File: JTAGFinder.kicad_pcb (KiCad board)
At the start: 4 copper layers, 90 x 70 mm, 95 parts, among them J1 Conn_02x05_Odd_Even, J10 V_drive, J2 Conn_02x05_Odd_Even, J3 LCD_IIC, J4 USB_C_Receptacle_USB2.0, J5 BT_HC08_SERIAL_COM, J6 Bus_PCI_Express_x1_free_pins_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, J7 GND, J8 GPIO_19-23, J9 +3V3, Q1 2N3904, SW1 SW_Push, U11 SN74S1051, U12 SN74S1051, U13 P8X32A-Q44, U2 M24512E-FMN6TP, U3 MIC2025-2YM, U4 FT232RL, U5 TLV74033, U6 USBLC6-2SC6, U7 AD8655, U8 LFS0108, U9 LFS0108, Y1 5MHz

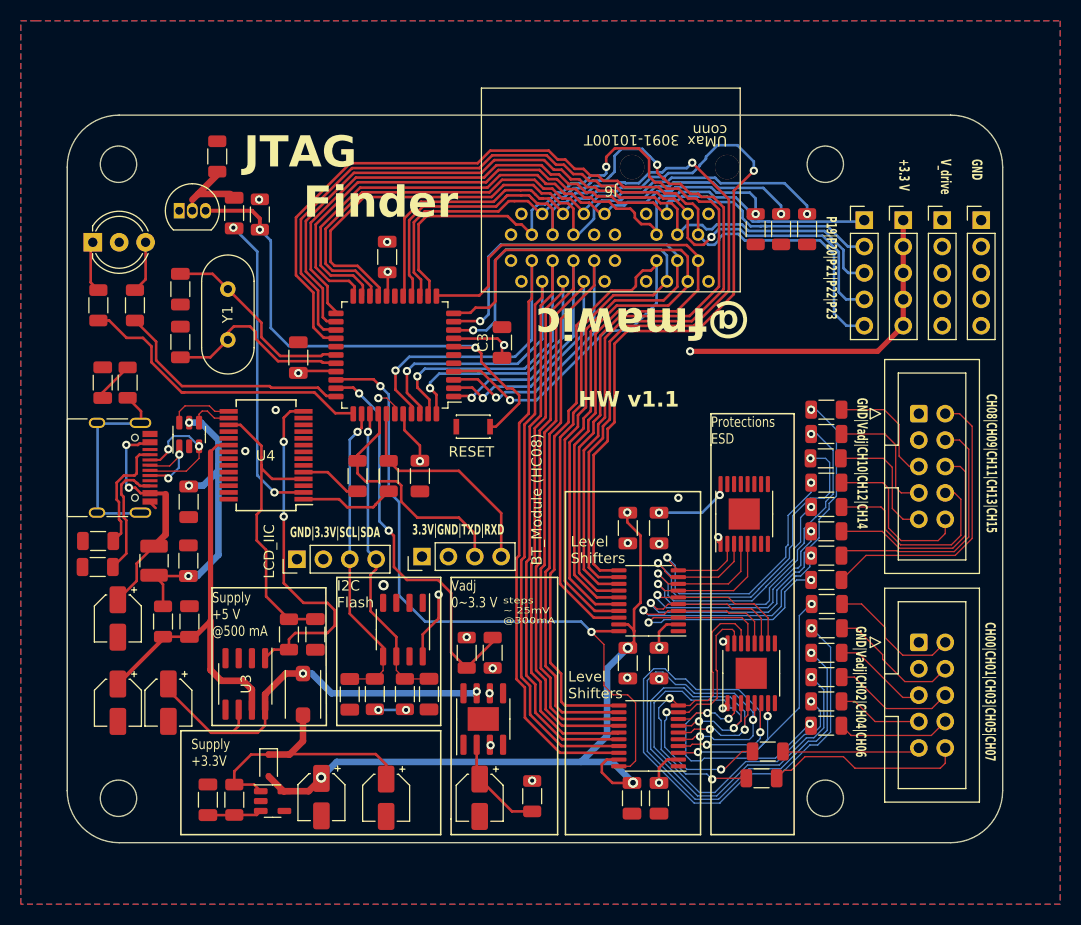
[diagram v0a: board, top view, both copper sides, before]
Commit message: update psu CI due thermal problems
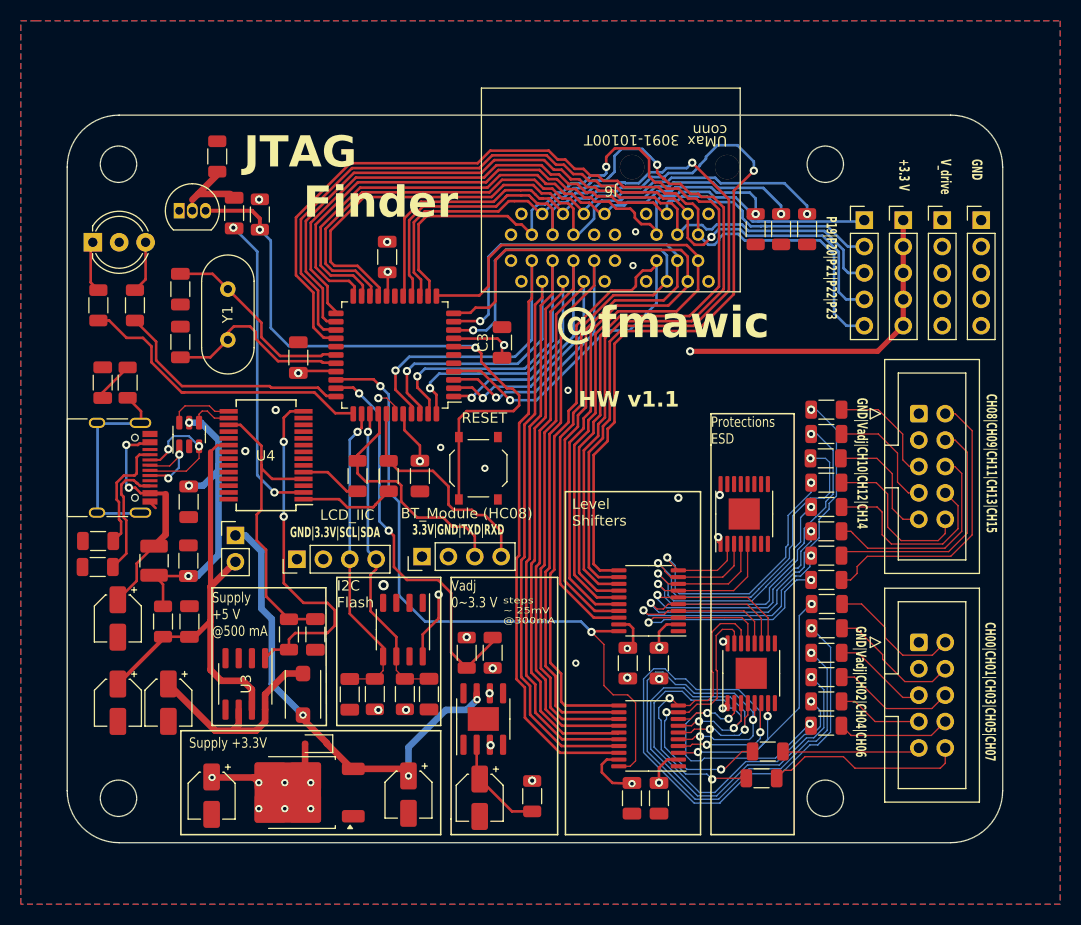
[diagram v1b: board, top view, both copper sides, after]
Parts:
- removed C13, C22, C25: 100nF, Capacitor_SMD:C_1206_3216Metric
- removed R6: 10k, Resistor_SMD:R_1206_3216Metric
- removed U5: TLV74033, Package_TO_SOT_SMD:SOT-23-5
- added J11: Conn_01x02, Connector_PinHeader_2.54mm:PinHeader_1x02_P2.54mm_Vertical, F.Cu at (120.2, 98.7)
- added U1: AP2114D-3.3TRG1, Package_TO_SOT_SMD:TO-252-2, F.Cu at (126.5, 123.5)
- C14: value 10uF -> 47uF
- SW1: footprint Button_Switch_SMD:SW_SPST_CK_KXT3 -> Button_Switch_SMD:SW_Push_1P1T_XKB_TS-1187A
- moved C14 10.6 mm to (118.0, 123.8)
- moved D1 5.01 mm to (128.0, 118.8), turned to 180 degrees
- moved SW1 4.03 mm to (143.6, 92.2), turned to 90 degrees
- moved C12 2.17 mm to (136.9, 123.7)
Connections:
- C11 pad 1: +5V -> Net-(C11-Pad1)
- C12 pad 1: Net-(D1-K) -> +5V
- D1 pad 1: Net-(D1-K) -> +5V
- L2 pad 1: +5V -> Net-(C11-Pad1)
- L2 pad 2: Net-(D1-K) -> +5V
- U3 pad 6: +5V -> Net-(C11-Pad1)
- U3 pad 8: +5V -> Net-(C11-Pad1)
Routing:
- net +3.3V: track 132.1 -> 78.8 mm, vias 13 -> 18
- net Net-(D1-K): track 25.5 -> 0.00 mm
- net Net-(C11-Pad1): track 0.00 -> 20.9 mm
- net /uController/ ~RES: track 50.2 -> 60.7 mm
- net VCC: track 41.3 -> 47.9 mm
- net Vdrive: track 17.0 -> 10.4 mm, vias 11 -> 10
- net +5V: track 39.5 -> 45.3 mm, vias 2 -> 3
- net Net-(U5-EN): track 5.25 -> 0.00 mm
- net /Protected Output/C13: track 19.6 -> 18.5 mm
- net /Protected Output/C11: track 21.4 -> 20.4 mm
- net /Protected Output/C12: track 12.2 -> 11.4 mm
- net /Protected Output/C09: track 24.1 -> 23.4 mm
- net GND: vias 11 -> 15
- added copper zone on In3.Cu, net GND
- added copper zone on In4.Cu, net Vdrive
- removed copper zone on In2.Cu, net Vdrive
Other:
- copper layers 4 -> 6

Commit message: back to 4 layer
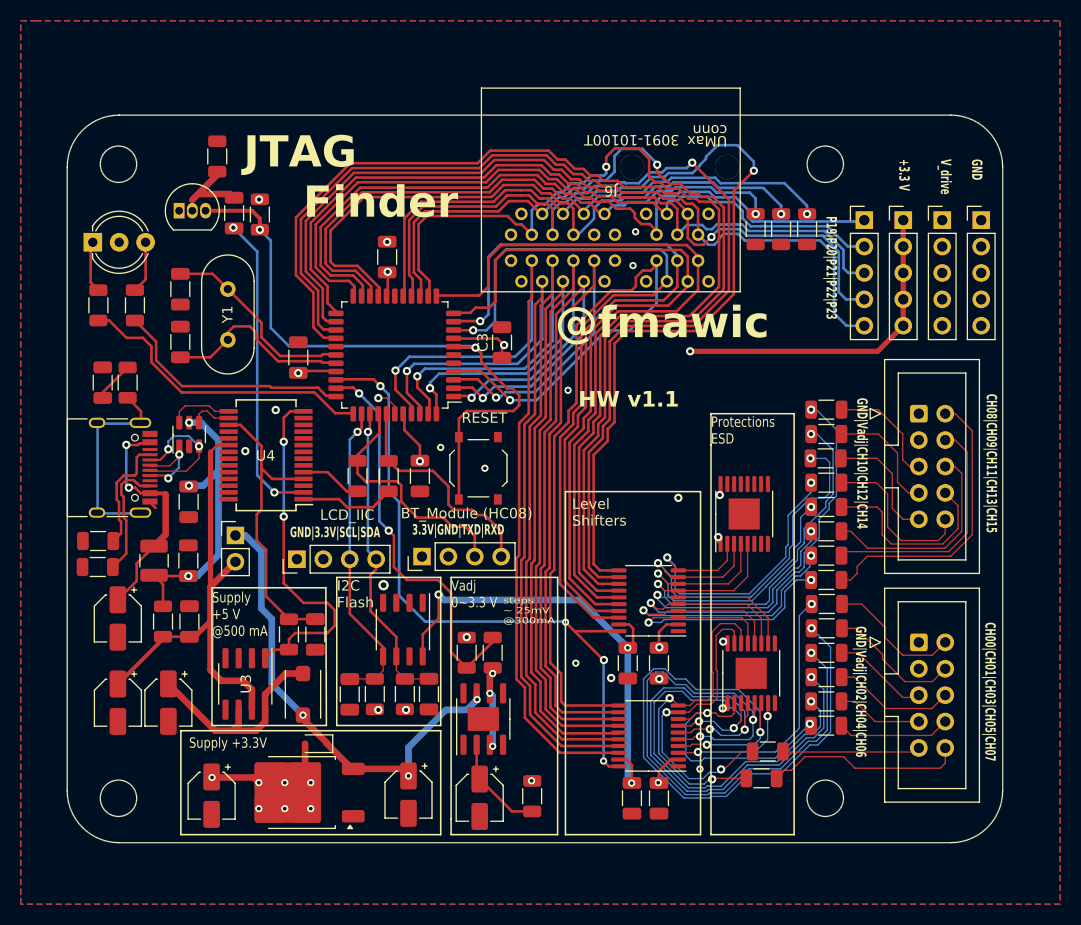
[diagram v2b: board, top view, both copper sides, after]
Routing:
- net +3.3V: track 78.8 -> 109.5 mm
- net Vdrive: track 10.4 -> 17.8 mm
- net TXSOE: track 64.7 -> 63.3 mm, vias 2 -> 4
- net CH00: track 28.9 -> 30.3 mm
- net CH06: track 28.2 -> 29.6 mm
- net CH07: track 30.6 -> 31.3 mm
- net CH05: track 26.4 -> 26.2 mm, vias 3 -> 2
- net GND: vias 15 -> 16
- added copper zone on In2.Cu, net Vdrive
- removed copper zone on In3.Cu, net GND
- removed copper zone on In4.Cu, net Vdrive
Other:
- copper layers 6 -> 4

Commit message: clock fix for FT232RL and update cleaner routes
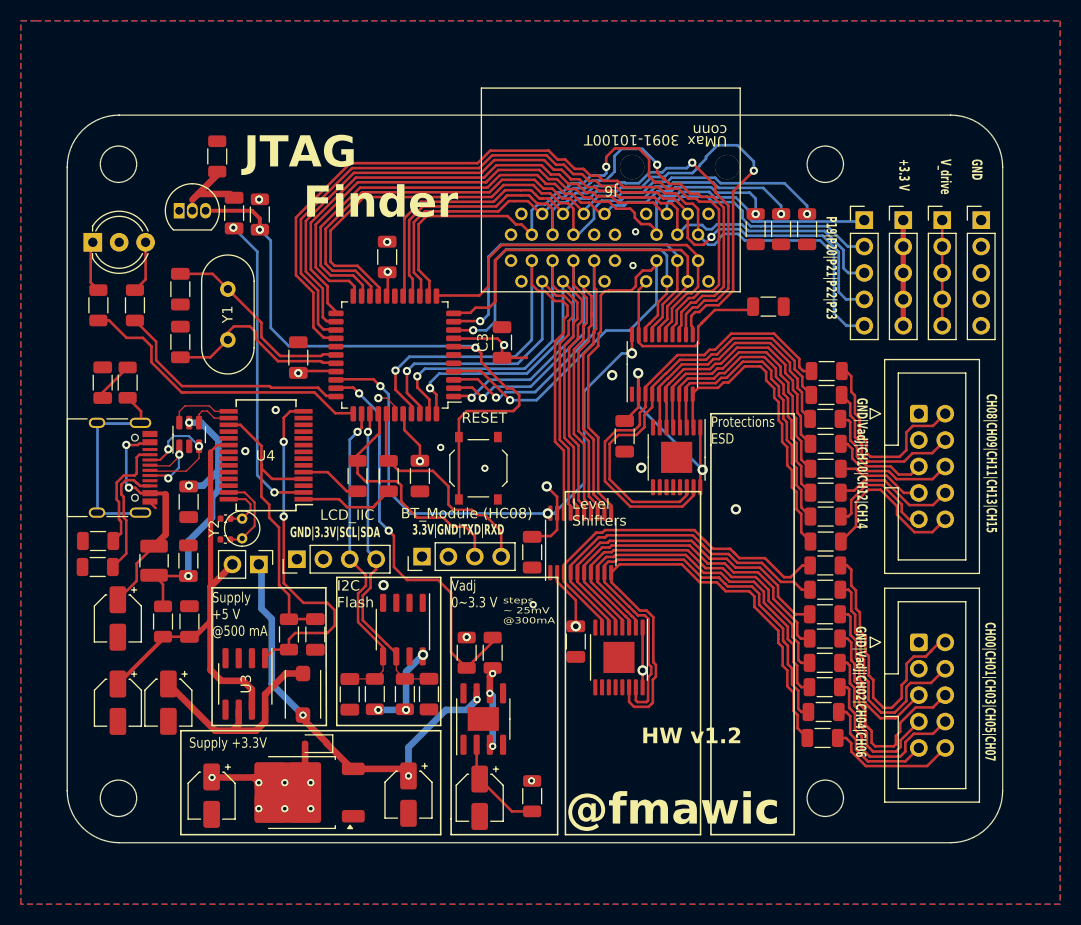
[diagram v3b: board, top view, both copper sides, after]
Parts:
- added C13: ~, Capacitor_SMD:C_0402_1005Metric, F.Cu at (119.3, 99.1)
- added C22: ~, Capacitor_SMD:C_0402_1005Metric, F.Cu at (119.3, 97.1)
- added Y2: 12MHz, Crystal:Crystal_C38-LF_D3.0mm_L8.0mm_Vertical, F.Cu at (120.9, 99.0)
- moved C21 36.9 mm to (171.5, 76.7), turned to 0 degrees
- moved C20 25.5 mm to (148.8, 100.3)
- moved U9 22.8 mm to (161.3, 82.3), turned to 90 degrees
- moved C24 22.1 mm to (157.7, 89.2)
- moved R23 20.1 mm to (177.1, 82.9)
- moved U8 19.7 mm to (153.5, 99.4), turned to 90 degrees
- moved C23 17.1 mm to (153.0, 108.9)
- moved R24 15.5 mm to (177.1, 85.2)
- moved U11 12.8 mm to (157.2, 110.5), turned to -90 degrees
- moved U12 8.48 mm to (162.7, 91.2), turned to -90 degrees
- moved R26 8.42 mm to (177.0, 89.9)
- moved R22 7.04 mm to (176.7, 118.2)
- moved R21 6.58 mm to (176.8, 115.7)
- moved R30 5.67 mm to (177.0, 99.3)
- moved R29 5.61 mm to (177.0, 96.9)
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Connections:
- U11 pad 10: CH11 -> unconnected-(U11-D07-Pad10)
- U11 pad 11: CH10 -> unconnected-(U11-D08-Pad11)
- U11 pad 12: CH09 -> unconnected-(U11-D09-Pad12)
- U11 pad 13: CH08 -> unconnected-(U11-D10-Pad13)
- U12 pad 14: unconnected-(U12-D11-Pad14) -> CH09
- U12 pad 15: unconnected-(U12-D12-Pad15) -> CH08
- U12 pad 6: unconnected-(U12-D05-Pad6) -> CH11
- U12 pad 7: unconnected-(U12-D06-Pad7) -> CH10
- U4 pad 27: unconnected-(U4-OSCI-Pad27) -> /USB_input_interface/x+
- U4 pad 28: unconnected-(U4-OSCO-Pad28) -> /USB_input_interface/x-
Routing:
- net P8: track 72.4 -> 35.8 mm
- net P9: track 73.1 -> 36.8 mm
- net Vdrive: track 17.8 -> 53.6 mm, vias 10 -> 8
- net P10: track 71.8 -> 36.6 mm
- net P11: track 73.2 -> 38.2 mm
- net P12: track 95.4 -> 61.3 mm
- net CH01: track 67.6 -> 33.9 mm, vias 3 -> 0
- net P13: track 93.1 -> 59.8 mm
- net P14: track 96.0 -> 63.6 mm
- net P15: track 98.5 -> 66.9 mm
- net +3.3V: track 109.5 -> 80.2 mm, vias 18 -> 16
- net P0: track 82.1 -> 54.1 mm
- net P1: track 77.1 -> 49.4 mm
- net P2: track 80.2 -> 53.0 mm
- net P3: track 74.6 -> 47.4 mm
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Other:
- board text added: "HW v1.2"
- board text removed: "HW v1.1"
